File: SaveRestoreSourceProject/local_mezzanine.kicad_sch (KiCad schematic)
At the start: 3 parts

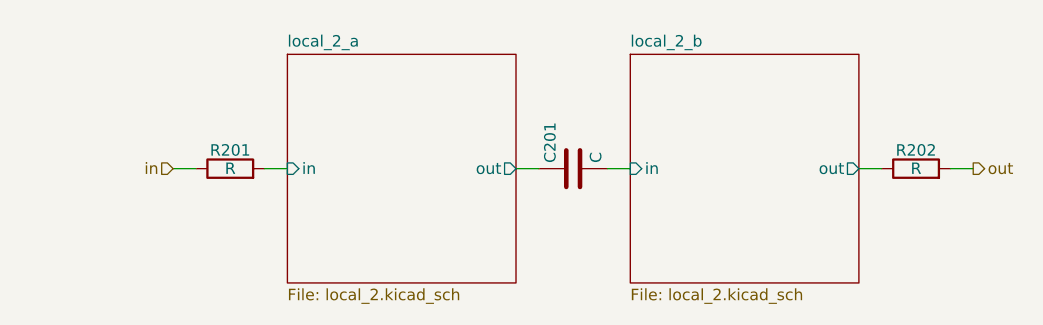
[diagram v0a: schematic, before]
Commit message: Add support for connected drawings, update test template
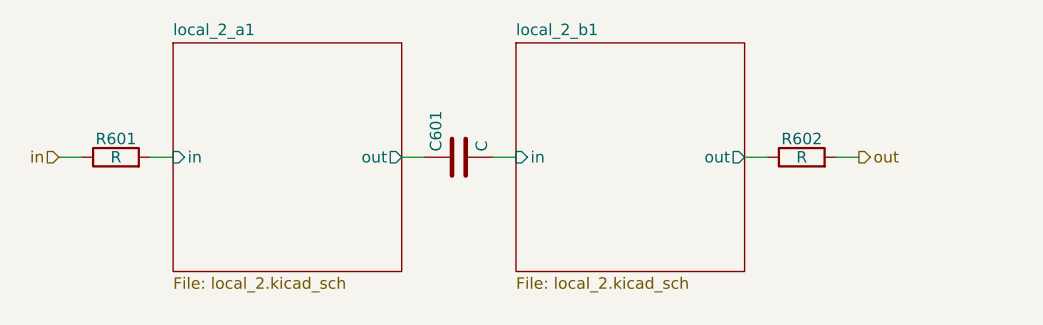
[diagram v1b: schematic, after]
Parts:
- removed C201: C, Capacitor_SMD:C_1206_3216Metric, symbol Device:C
- removed R201, R202: R, Resistor_SMD:R_1206_3216Metric, symbol Device:R
- added C601: C, Capacitor_SMD:C_1206_3216Metric, symbol Device:C
- added R601, R602: R, Resistor_SMD:R_1206_3216Metric, symbol Device:R
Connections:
- net in: now also R601.1
- net out: now also R602.2
- new net local_2_a1/in: R601.2
- new net local_2_a1/out: C601.1
- new net local_2_b1/in: C601.2
- new net local_2_b1/out: R602.1
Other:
- removed sheet local_2_a
- removed sheet local_2_b
- added sheet local_2_a1 (local_2.kicad_sch)
- added sheet local_2_b1 (local_2.kicad_sch)
